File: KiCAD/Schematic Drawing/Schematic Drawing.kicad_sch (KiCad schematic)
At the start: 11 parts, among them M1 Motor_Servo, M2 Motor_Servo, U1 ESP32-WROOM-32

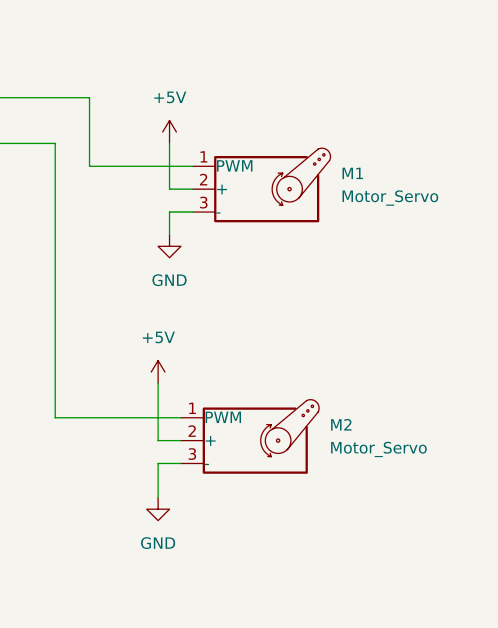
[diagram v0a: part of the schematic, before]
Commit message: updated values in schematic
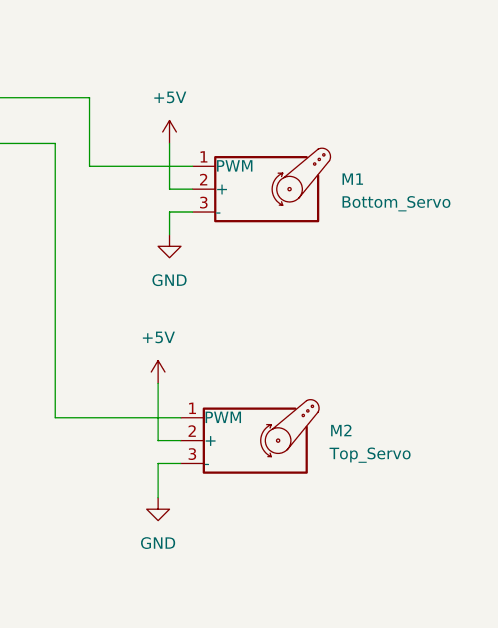
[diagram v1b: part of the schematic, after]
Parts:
- M1: value Motor_Servo -> Bottom_Servo
- M2: value Motor_Servo -> Top_Servo
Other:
- title: (none) -> Schematic of Smart Solar Panel
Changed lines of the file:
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@@
 (kicad_sch (version 20230121) (generator eeschema)
   (paper "A4")
+  (title_block
+    (title "Schematic of Smart Solar Panel")
+  )
   (junction (at 168.91 95.25) (diameter 0) (color 0 0 0 0)
   )
@@
   (symbol (lib_id "Motor:Motor_Servo") (at 236.22 72.39 0) (unit 1)
     (in_bom yes) (on_board yes) (dnp no) (fields_autoplaced)
-    (property "Reference" "M1" (at 245.11 70.6866 0)
-      (effects (font (size 1.27 1.27)) (justify left))
-    )
-    (property "Value" "Motor_Servo" (at 245.11 73.2266 0)
+    (property "Reference" "M1" (at 245.11 71.3216 0)
+      (effects (font (size 1.27 1.27)) (justify left))
+    )
+    (property "Value" "Bottom_Servo" (at 245.11 73.8616 0)
       (effects (font (size 1.27 1.27)) (justify left))
     )
@@
   (symbol (lib_id "Motor:Motor_Servo") (at 234.95 100.33 0) (unit 1)
     (in_bom yes) (on_board yes) (dnp no) (fields_autoplaced)
-    (property "Reference" "M2" (at 243.84 98.6266 0)
-      (effects (font (size 1.27 1.27)) (justify left))
-    )
-    (property "Value" "Motor_Servo" (at 243.84 101.1666 0)
-      (effects (font (size 1.27 1.27)) (justify left))
-    )
+    (property "Reference" "M2" (at 243.84 99.2616 0)
+      (effects (font (size 1.27 1.27)) (justify left))
+    )
+    (property "Value" "Top_Servo" (at 243.84 101.8016 0)
+      (effects (font (size 1.27 1.27)) (justify left))
+    )

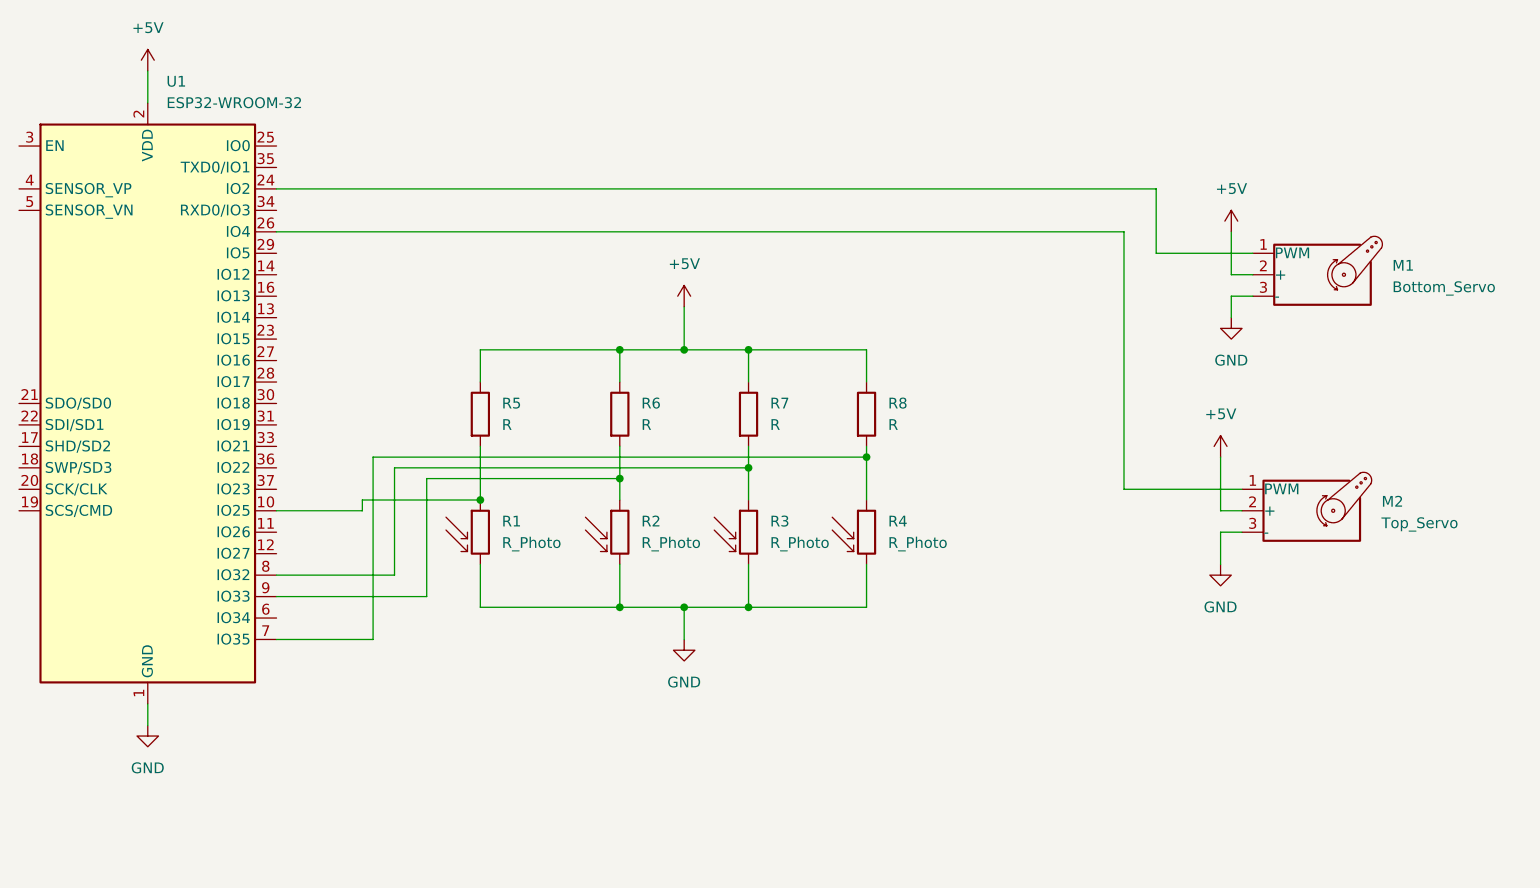
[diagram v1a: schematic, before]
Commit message: added powerswitch
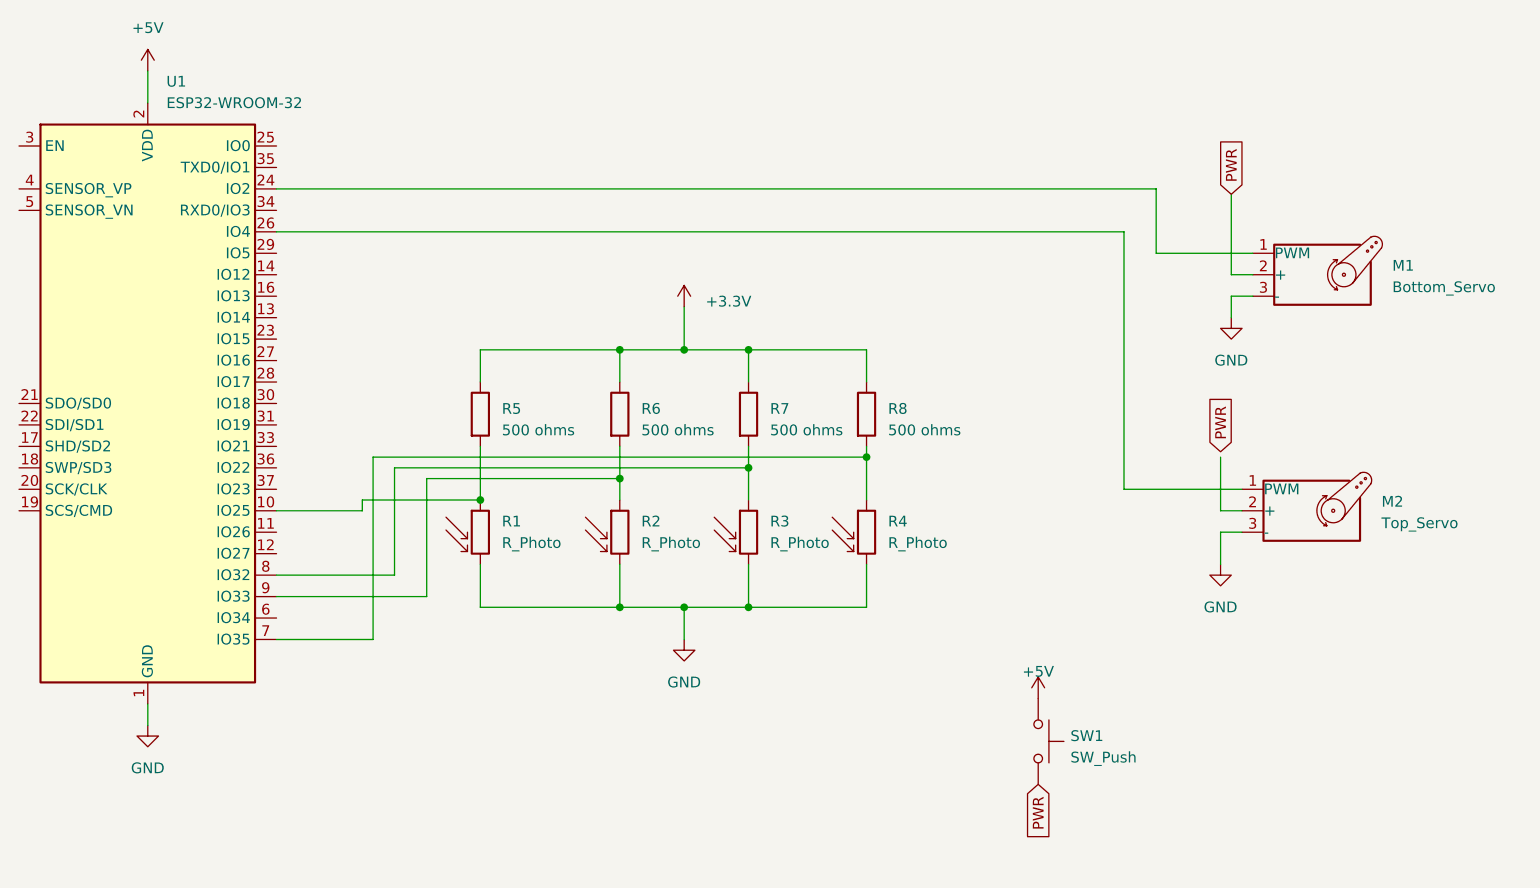
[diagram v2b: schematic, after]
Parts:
- added SW1: SW_Push, symbol Switch:SW_Push
- R5, R6, R7, R8: value R -> 500 ohms
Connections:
- net +5V: now also SW1.1; no longer M1.2 (+), M2.2 (+)
- new net PWR: M1.2 (+), SW1.2
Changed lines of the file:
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@@
     (stroke (width 0) (type default))
   )
-  (wire (pts (xy 226.06 67.31) (xy 226.06 72.39))
+  (wire (pts (xy 226.06 62.865) (xy 226.06 72.39))
     (stroke (width 0) (type default))
   )
@@
     (stroke (width 0) (type default))
   )
-  (symbol (lib_id "power:+5V") (at 226.06 67.31 0) (unit 1)
-    (in_bom yes) (on_board yes) (dnp no) (fields_autoplaced)
-    (property "Reference" "#PWR08" (at 226.06 71.12 0)
-      (effects (font (size 1.27 1.27)) hide)
-    )
-    (property "Value" "+5V" (at 226.06 62.23 0)
+  (global_label "PWR" (shape input) (at 226.06 62.865 90) (fields_autoplaced)
+    (effects (font (size 1.27 1.27)) (justify left))
+    (property "Intersheetrefs" "${INTERSHEET_REFS}" (at 226.06 55.9678 90)
+      (effects (font (size 1.27 1.27)) (justify left) hide)
+    )
+  )
+  (global_label "PWR" (shape input) (at 203.2 132.715 270) (fields_autoplaced)
+    (effects (font (size 1.27 1.27)) (justify right))
+    (property "Intersheetrefs" "${INTERSHEET_REFS}" (at 203.2 139.6122 90)
+      (effects (font (size 1.27 1.27)) (justify right) hide)
+    )
+  )
+  (global_label "PWR" (shape input) (at 224.79 93.345 90) (fields_autoplaced)
+    (effects (font (size 1.27 1.27)) (justify left))
+    (property "Intersheetrefs" "${INTERSHEET_REFS}" (at 224.79 86.4478 90)
+      (effects (font (size 1.27 1.27)) (justify left) hide)
+    )
+  )
+  (symbol (lib_id "power:+5V") (at 203.2 122.555 0) (unit 1)
+    (in_bom yes) (on_board yes) (dnp no) (fields_autoplaced)
+    (property "Reference" "#PWR09" (at 203.2 126.365 0)
+      (effects (font (size 1.27 1.27)) hide)
+    )
+    (property "Value" "+5V" (at 203.2 119.38 0)
       (effects (font (size 1.27 1.27)))
     )
-    (property "Footprint" "" (at 226.06 67.31 0)
-      (effects (font (size 1.27 1.27)) hide)
-    )
-    (property "Datasheet" "" (at 226.06 67.31 0)
-      (effects (font (size 1.27 1.27)) hide)
-    )
-    (pin "1")
-    (instances
-      (project "Schematic Drawing"
-        (path "/0ed5c89d-5ee1-4815-a35d-cea572580a56"
-          (reference "#PWR08") (unit 1)
+    (property "Footprint" "" (at 203.2 122.555 0)
+      (effects (font (size 1.27 1.27)) hide)
+    )
+    (property "Datasheet" "" (at 203.2 122.555 0)
+      (effects (font (size 1.27 1.27)) hide)
+    )
+    (pin "1")
+    (instances
+      (project "Schematic Drawing"
+        (path "/0ed5c89d-5ee1-4815-a35d-cea572580a56"
+          (reference "#PWR09") (unit 1)
         )
       )
@@
     )
   )
-  (symbol (lib_id "power:+5V") (at 224.79 93.98 0) (unit 1)
-    (in_bom yes) (on_board yes) (dnp no) (fields_autoplaced)
-    (property "Reference" "#PWR07" (at 224.79 97.79 0)
-      (effects (font (size 1.27 1.27)) hide)
-    )
-    (property "Value" "+5V" (at 224.79 88.9 0)
-      (effects (font (size 1.27 1.27)))
-    )
-    (property "Footprint" "" (at 224.79 93.98 0)
-      (effects (font (size 1.27 1.27)) hide)
-    )
-    (property "Datasheet" "" (at 224.79 93.98 0)
-      (effects (font (size 1.27 1.27)) hide)
-    )
-    (pin "1")
-    (instances
-      (project "Schematic Drawing"
-        (path "/0ed5c89d-5ee1-4815-a35d-cea572580a56"
-          (reference "#PWR07") (unit 1)
-        )
-      )
-    )
-  )
   (symbol (lib_id "power:GND") (at 97.79 125.73 0) (unit 1)
     (in_bom yes) (on_board yes) (dnp no) (fields_autoplaced)
@@
       (effects (font (size 1.27 1.27)) hide)
     )
-    (property "Value" "+5V" (at 161.29 71.12 0)
-      (effects (font (size 1.27 1.27)))
+    (property "Value" "+3.3V" (at 163.83 75.565 0)
+      (effects (font (size 1.27 1.27)) (justify left))
     )
     (property "Footprint" "" (at 161.29 76.2 0)
@@
   (symbol (lib_id "Device:R") (at 137.16 88.9 0) (unit 1)
     (in_bom yes) (on_board yes) (dnp no) (fields_autoplaced)
-    (property "Reference" "R5" (at 139.7 87.63 0)
-      (effects (font (size 1.27 1.27)) (justify left))
-    )
-    (property "Value" "R" (at 139.7 90.17 0)
+    (property "Reference" "R5" (at 139.7 88.265 0)
+      (effects (font (size 1.27 1.27)) (justify left))
+    )
+    (property "Value" "500 ohms" (at 139.7 90.805 0)
       (effects (font (size 1.27 1.27)) (justify left))
     )
@@
   (symbol (lib_id "Device:R") (at 153.67 88.9 0) (unit 1)
     (in_bom yes) (on_board yes) (dnp no) (fields_autoplaced)
-    (property "Reference" "R6" (at 156.21 87.63 0)
-      (effects (font (size 1.27 1.27)) (justify left))
-    )
-    (property "Value" "R" (at 156.21 90.17 0)
+    (property "Reference" "R6" (at 156.21 88.265 0)
+      (effects (font (size 1.27 1.27)) (justify left))
+    )
+    (property "Value" "500 ohms" (at 156.21 90.805 0)
       (effects (font (size 1.27 1.27)) (justify left))
     )
@@
   (symbol (lib_id "Device:R") (at 182.88 88.9 0) (unit 1)
     (in_bom yes) (on_board yes) (dnp no) (fields_autoplaced)
-    (property "Reference" "R8" (at 185.42 87.63 0)
-      (effects (font (size 1.27 1.27)) (justify left))
-    )
-    (property "Value" "R" (at 185.42 90.17 0)
+    (property "Reference" "R8" (at 185.42 88.265 0)
+      (effects (font (size 1.27 1.27)) (justify left))
+    )
+    (property "Value" "500 ohms" (at 185.42 90.805 0)
       (effects (font (size 1.27 1.27)) (justify left))
     )
@@
         (path "/0ed5c89d-5ee1-4815-a35d-cea572580a56"
           (reference "#PWR05") (unit 1)
+        )
+      )
+    )
+  )
+  (symbol (lib_id "Switch:SW_Push") (at 203.2 127.635 270) (unit 1)
+    (in_bom yes) (on_board yes) (dnp no) (fields_autoplaced)
+    (property "Reference" "SW1" (at 207.01 127 90)
+      (effects (font (size 1.27 1.27)) (justify left))
+    )
+    (property "Value" "SW_Push" (at 207.01 129.54 90)
+      (effects (font (size 1.27 1.27)) (justify left))
+    )
+    (property "Footprint" "" (at 208.28 127.635 0)
+      (effects (font (size 1.27 1.27)) hide)
+    )
+    (property "Datasheet" "~" (at 208.28 127.635 0)
+      (effects (font (size 1.27 1.27)) hide)
+    )
+    (pin "1")
+    (pin "2")
+    (instances
+      (project "Schematic Drawing"
+        (path "/0ed5c89d-5ee1-4815-a35d-cea572580a56"
+          (reference "SW1") (unit 1)
         )
       )
@@
   (symbol (lib_id "Device:R") (at 168.91 88.9 0) (unit 1)
     (in_bom yes) (on_board yes) (dnp no) (fields_autoplaced)
-    (property "Reference" "R7" (at 171.45 87.63 0)
-      (effects (font (size 1.27 1.27)) (justify left))
-    )
-    (property "Value" "R" (at 171.45 90.17 0)
-      (effects (font (size 1.27 1.27)) (justify left))
-    )
+    (property "Reference" "R7" (at 171.45 88.265 0)
+      (effects (font (size 1.27 1.27)) (justify left))
+    )
+    (property "Value" "500 ohms" (at 171.45 90.805 0)
+      (effects (font (size 1.27 1.27)) (justify left))
+    )

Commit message: made proj library, added power switch symbol
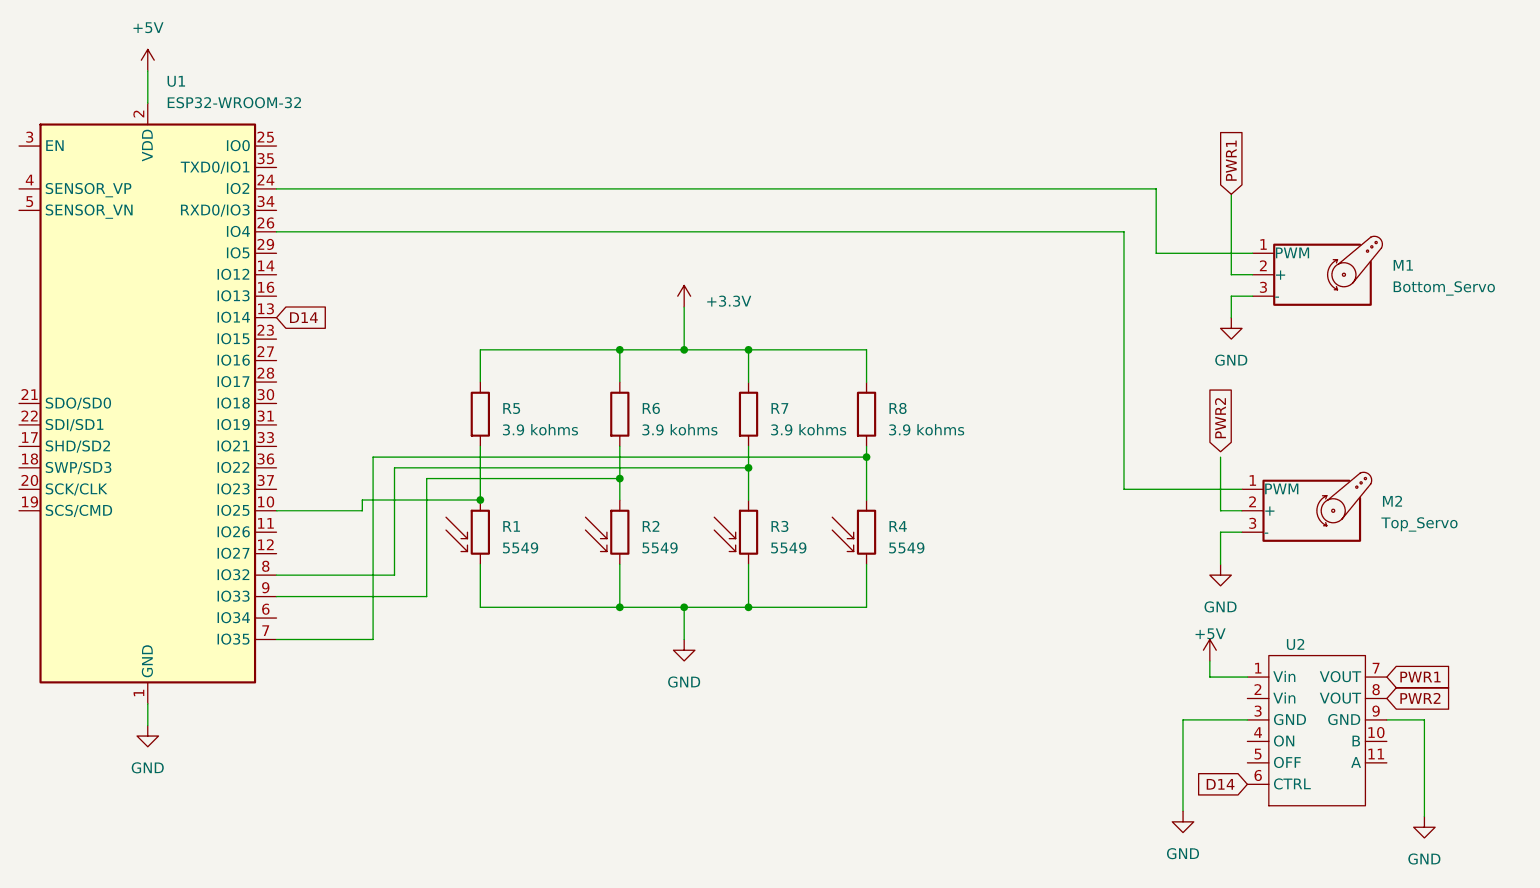
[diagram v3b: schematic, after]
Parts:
- removed SW1: SW_Push, symbol Switch:SW_Push
- added U2: ~, symbol my_lib:power_switch
- R1, R2, R3, R4: value R_Photo -> 5549
- R5, R6, R7, R8: value 500 ohms -> 3.9 kohms
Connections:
- net +5V: now also U2.1 (Vin)
- net GND: now also U2.3 (GND), U2.9 (GND)
- net D14: now reaches U1.13 (IO14)
- net D14: now also U2.6 (CTRL)
- net PWR renamed PWR1
- net PWR1: now also U2.7 (VOUT)
- new net PWR2: U2.8 (VOUT)

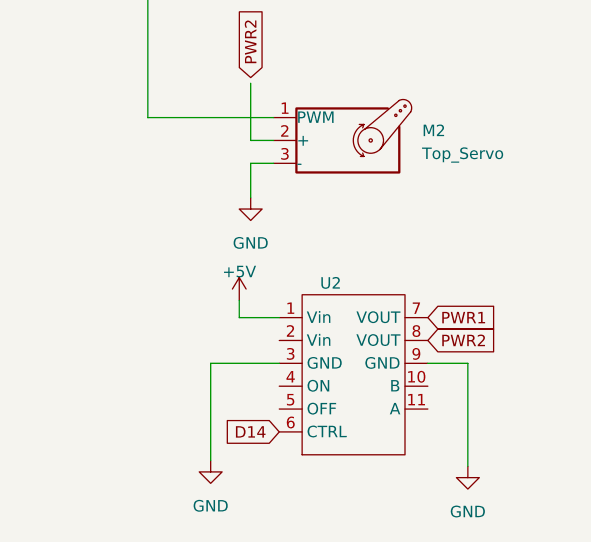
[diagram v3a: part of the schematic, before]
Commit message: gave more clarity
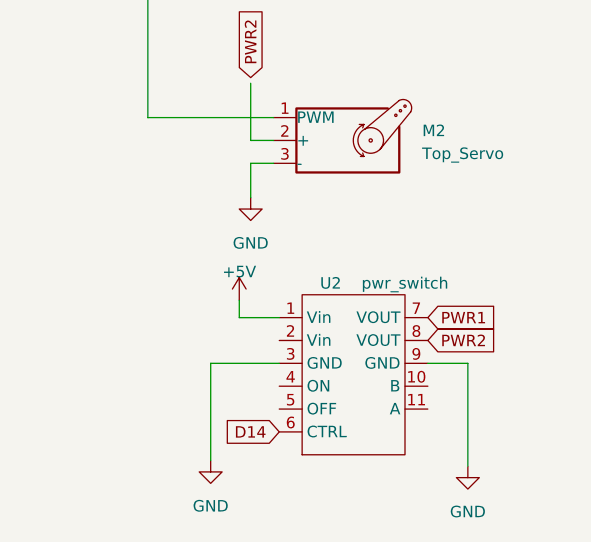
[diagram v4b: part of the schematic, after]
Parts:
- U2: value ~ -> pwr_switch
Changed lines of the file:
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@@
       (effects (font (size 1.27 1.27)))
     )
-    (property "Value" "~" (at 230.505 125.095 0)
+    (property "Value" "pwr_switch" (at 241.935 116.205 0)
       (effects (font (size 1.27 1.27)))
     )
